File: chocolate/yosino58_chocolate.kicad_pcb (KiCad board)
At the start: 2 copper layers, 157.8 x 135.3 mm, 121 parts, among them J0 LED, J1 TRRS, J2 OLED, J3 OLED, J4 OLED, J5 OLED, J6 OLED, P1 i2c_pin, P2 i2c_pin, SW1 SW_PUSH, SW10 SW_PUSH, SW11 SW_PUSH, SW12 SW_PUSH, SW13 SW_PUSH, SW14 SW_PUSH, SW15 SW_PUSH, SW16 SW_PUSH, SW17 SW_PUSH, SW18 SW_PUSH, SW19 SW_PUSH, SW2 SW_PUSH, SW20 SW_PUSH, SW21 SW_PUSH, SW22 SW_PUSH, SW23 SW_PUSH, SW24 SW_PUSH, SW25 SW_PUSH, SW26 SW_PUSH, SW27 SW_PUSH, SW28 SW_PUSH, SW29 SW_PUSH, SW3 SW_PUSH, SW4 SW_PUSH, SW5 SW_PUSH, SW6 SW_PUSH, SW7 SW_PUSH, SW8 SW_PUSH, SW9 SW_PUSH, U1 ProMicro, U2 ProMicro

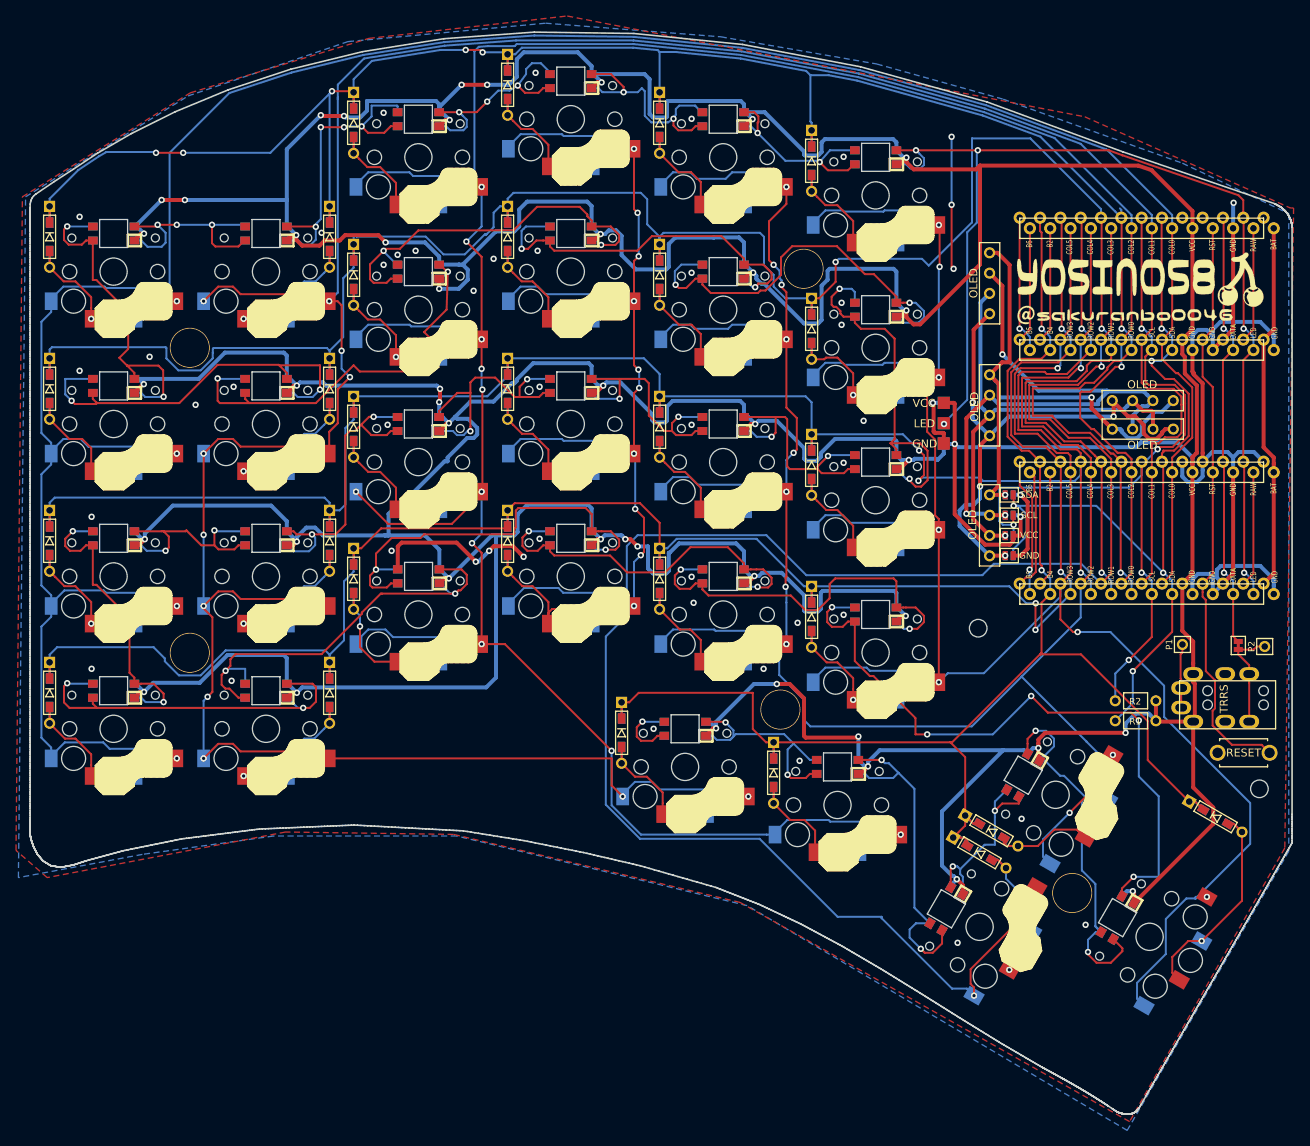
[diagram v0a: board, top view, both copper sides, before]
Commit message: 基本外形修正
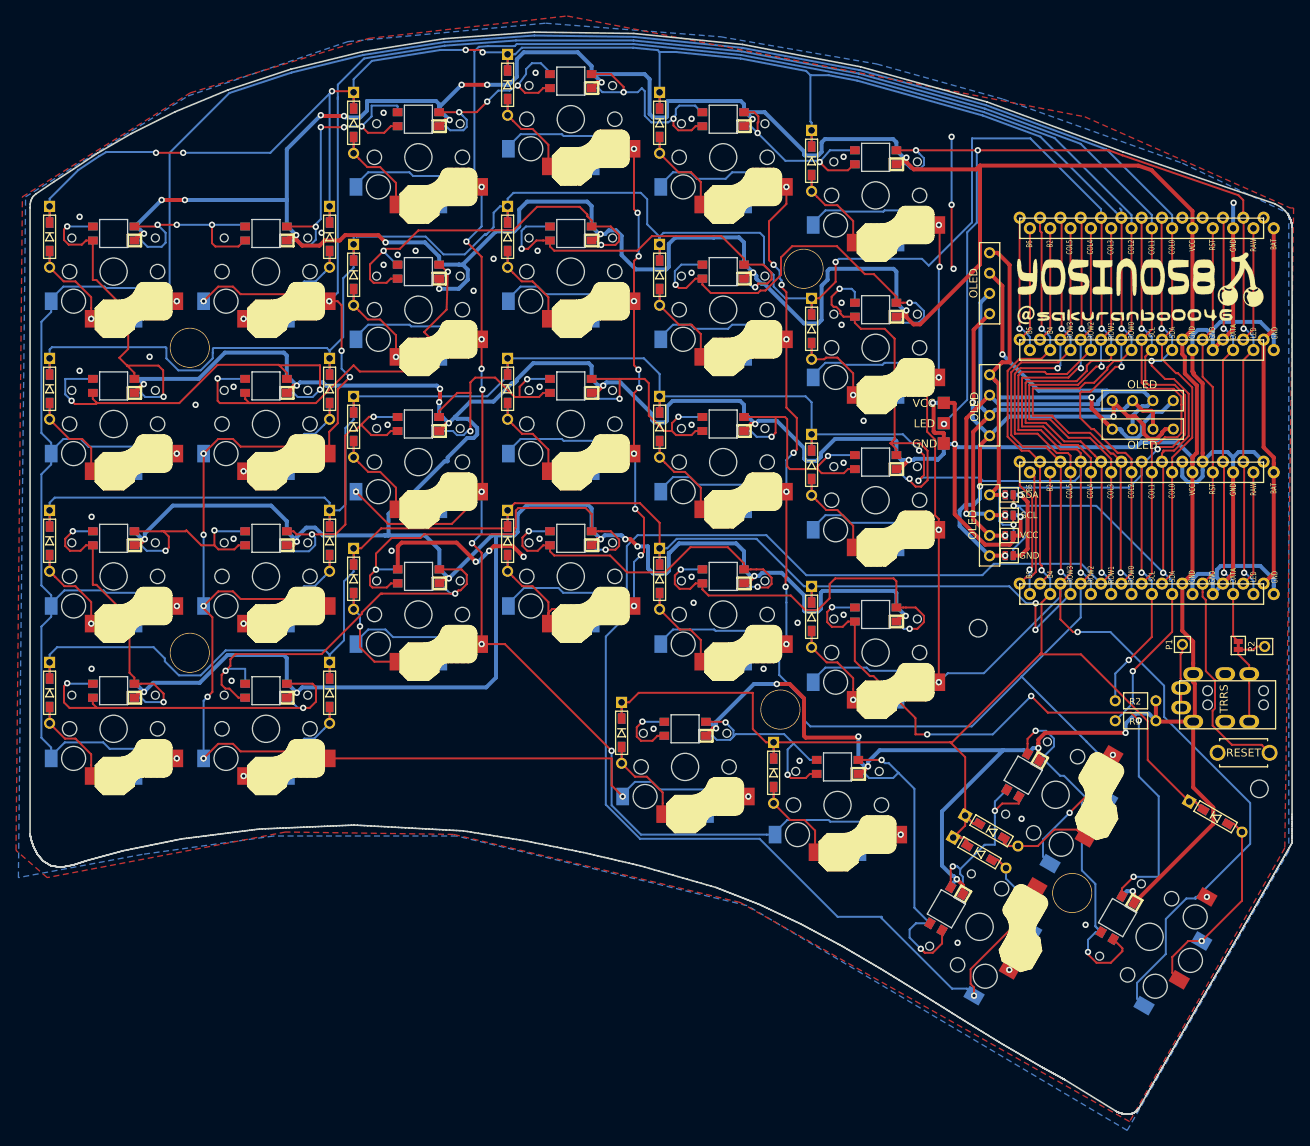
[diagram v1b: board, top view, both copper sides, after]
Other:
- outline, holes or cut-outs redrawn
